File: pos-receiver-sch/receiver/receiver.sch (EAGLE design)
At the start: 17 parts, among them IC1 AD8599R

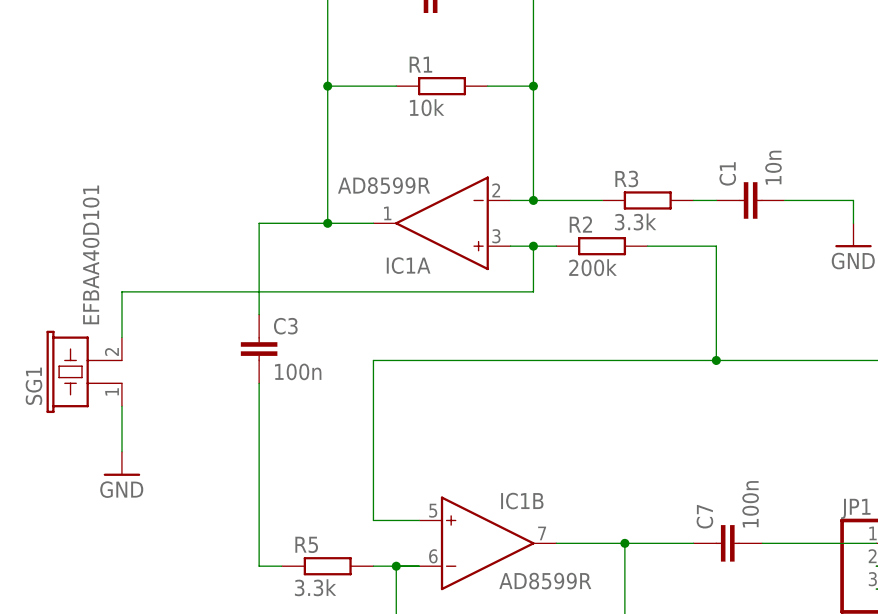
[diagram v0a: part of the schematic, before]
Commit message: zmiany w schemacie
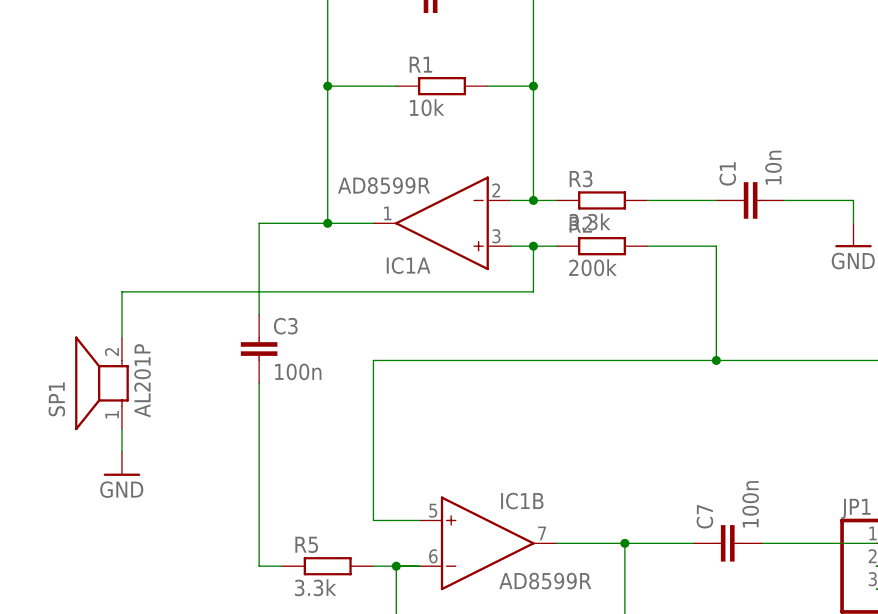
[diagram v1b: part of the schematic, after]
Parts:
- removed SG1: EFBAA40D101, buzzer:EFBAA40D101
- added SP1: AL201P, buzzer:AL201P
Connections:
- net GND: now also SP1.1; no longer SG1.1
- net N$7: now also SP1.2; no longer SG1.2
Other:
- moved on the sheet: R3
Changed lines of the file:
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@@
 <part name="GND4" library="supply1" deviceset="GND" device=""/>
 <part name="GND5" library="supply1" deviceset="GND" device=""/>
-<part name="SG1" library="buzzer" deviceset="EFB?" device="AA40D101"/>
 <part name="GND6" library="supply1" deviceset="GND" device=""/>
 <part name="SUPPLY1" library="supply2" deviceset="VCC" device=""/>
@@
 <part name="GND8" library="supply1" deviceset="GND" device=""/>
 <part name="C7" library="resistor" deviceset="C-EU" device="C1206" value="100n"/>
+<part name="SP1" library="buzzer" deviceset="AL201P" device=""/>
 </parts>
 <sheets>
@@
 <instance part="R1" gate="G$1" x="35.56" y="83.82"/>
 <instance part="R2" gate="G$1" x="53.34" y="66.04"/>
-<instance part="R3" gate="G$1" x="58.42" y="71.12"/>
+<instance part="R3" gate="G$1" x="53.34" y="71.12"/>
 <instance part="R4" gate="G$1" x="40.64" y="17.78"/>
 <instance part="R5" gate="G$1" x="22.86" y="30.48"/>
@@
 <instance part="GND4" gate="1" x="147.32" y="33.02"/>
 <instance part="GND5" gate="1" x="157.48" y="33.02"/>
-<instance part="SG1" gate="G$1" x="-2.54" y="50.8" rot="R90"/>
 <instance part="GND6" gate="1" x="0" y="40.64"/>
 <instance part="SUPPLY1" gate="G$1" x="157.48" y="86.36"/>
@@
 <instance part="GND8" gate="1" x="139.7" y="33.02"/>
 <instance part="C7" gate="G$1" x="66.04" y="33.02" rot="R90"/>
+<instance part="SP1" gate="G$1" x="0" y="50.8" rot="R90"/>
 </instances>
 <busses>
@@
 <wire x1="43.18" y1="71.12" x2="45.72" y2="71.12" width="0.1524" layer="91"/>
 <pinref part="C2" gate="G$1" pin="2"/>
-<wire x1="45.72" y1="71.12" x2="53.34" y2="71.12" width="0.1524" layer="91"/>
+<wire x1="45.72" y1="71.12" x2="48.26" y2="71.12" width="0.1524" layer="91"/>
 <wire x1="38.1" y1="93.98" x2="45.72" y2="93.98" width="0.1524" layer="91"/>
 <wire x1="45.72" y1="93.98" x2="45.72" y2="83.82" width="0.1524" layer="91"/>
@@
 <pinref part="R3" gate="G$1" pin="2"/>
 <pinref part="C1" gate="G$1" pin="1"/>
-<wire x1="63.5" y1="71.12" x2="66.04" y2="71.12" width="0.1524" layer="91"/>
+<wire x1="58.42" y1="71.12" x2="66.04" y2="71.12" width="0.1524" layer="91"/>
 </segment>
 </net>
@@
 <wire x1="73.66" y1="71.12" x2="81.28" y2="71.12" width="0.1524" layer="91"/>
 <wire x1="81.28" y1="71.12" x2="81.28" y2="68.58" width="0.1524" layer="91"/>
-</segment>
-<segment>
-<pinref part="GND6" gate="1" pin="GND"/>
-<pinref part="SG1" gate="G$1" pin="1"/>
-<wire x1="0" y1="43.18" x2="0" y2="48.26" width="0.1524" layer="91"/>
 </segment>
 <segment>
@@
 <pinref part="GND8" gate="1" pin="GND"/>
 <wire x1="139.7" y1="50.8" x2="139.7" y2="35.56" width="0.1524" layer="91"/>
+</segment>
+<segment>
+<pinref part="GND6" gate="1" pin="GND"/>
+<pinref part="SP1" gate="G$1" pin="1"/>
+<wire x1="0" y1="43.18" x2="0" y2="45.72" width="0.1524" layer="91"/>
 </segment>
 </net>
@@
 <pinref part="R2" gate="G$1" pin="1"/>
 <wire x1="48.26" y1="66.04" x2="45.72" y2="66.04" width="0.1524" layer="91"/>
-<pinref part="SG1" gate="G$1" pin="2"/>
 <wire x1="45.72" y1="66.04" x2="43.18" y2="66.04" width="0.1524" layer="91"/>
-<wire x1="0" y1="55.88" x2="0" y2="60.96" width="0.1524" layer="91"/>
 <wire x1="0" y1="60.96" x2="45.72" y2="60.96" width="0.1524" layer="91"/>
 <wire x1="45.72" y1="60.96" x2="45.72" y2="66.04" width="0.1524" layer="91"/>
 <junction x="45.72" y="66.04"/>
+<pinref part="SP1" gate="G$1" pin="2"/>
+<wire x1="0" y1="55.88" x2="0" y2="60.96" width="0.1524" layer="91"/>
 </segment>
 </net>

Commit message: receiver-sch ver: 0.2
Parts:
- added C8: 100p, resistor:C-EUC1206K
- added IC2: 78L10F, linear:78L10F
- C2: value 22p -> 100p
- R1, R4: value 10k -> 33k
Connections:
- new net N$10: C5.1, IC2.VI, JP1.2
- net GND: now also IC2.GND, IC2.GND@1
- net N$4: now also C8.1
- net N$5: now also C8.2
- net VCC: now also IC2.VO; no longer C5.1, JP1.2
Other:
- moved on the sheet: C4, C5, C6, IC1P, JP1, R3, R6, R7

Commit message: charge amp
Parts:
- removed C1: 10n, resistor:C-EUC1206K
- removed IC2: 78L10F, linear:78L10F
- removed R2: 200k, resistor:R-EU_R0805
- removed R3: 3.3k, resistor:R-EU_R0805
- C7: device resistor:C-EUC1206 -> resistor:C-EUC1206K
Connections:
- removed net N$10: C5.1, IC2.VI, JP1.2
- removed net N$2: C2.2, IC1A.IN-, R1.2, R3.1
- removed net N$7: IC1A.IN+, R2.1, SP1.2
- net GND: no longer C1.2, IC2.GND, IC2.GND@1, SP1.1
- net N$3: now also C2.2, IC1A.IN-, R1.2, SP1.1; no longer C1.1, R3.2
- net N$9: now also IC1A.IN+, SP1.2; no longer R2.2
- net VCC: now also C5.1, JP1.2; no longer IC2.VO
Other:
- moved on the sheet: SP1

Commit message: pcb
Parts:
- C2: value 100p -> 12p; device resistor:C-EUC1206K -> resistor:C-EUC0805
- C3, C4, C5, C8: device resistor:C-EUC1206K -> resistor:C-EUC0805
- IC1: value AD8599R -> NE5532D; device analog-devices:AD8599R -> linear:NE5532D
- R1: value 33k -> 1M
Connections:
- net N$3: now also IC1A.-IN; no longer IC1A.IN-
- net N$4: now also IC1B.-IN; no longer IC1B.IN-
- net N$9: now also IC1A.+IN, IC1B.+IN; no longer IC1A.IN+, IC1B.IN+
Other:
- moved on the sheet: C8, IC1B, R4
